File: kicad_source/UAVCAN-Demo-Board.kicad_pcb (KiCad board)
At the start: 2 copper layers, 91.4 x 50.8 mm, 38 parts, among them CN1 ARDUINO_NANO_33, CN2 691322310004, CN3 GH_SM04B-GHS-TB, CN4 GH_SM04B-GHS-TB, CN5 691322310004, CN6 691322310004, SW1 TAST_VER, U1 MCP2515, U2 SN65VHD232, U3 DS18B20, Y1 16 MHz

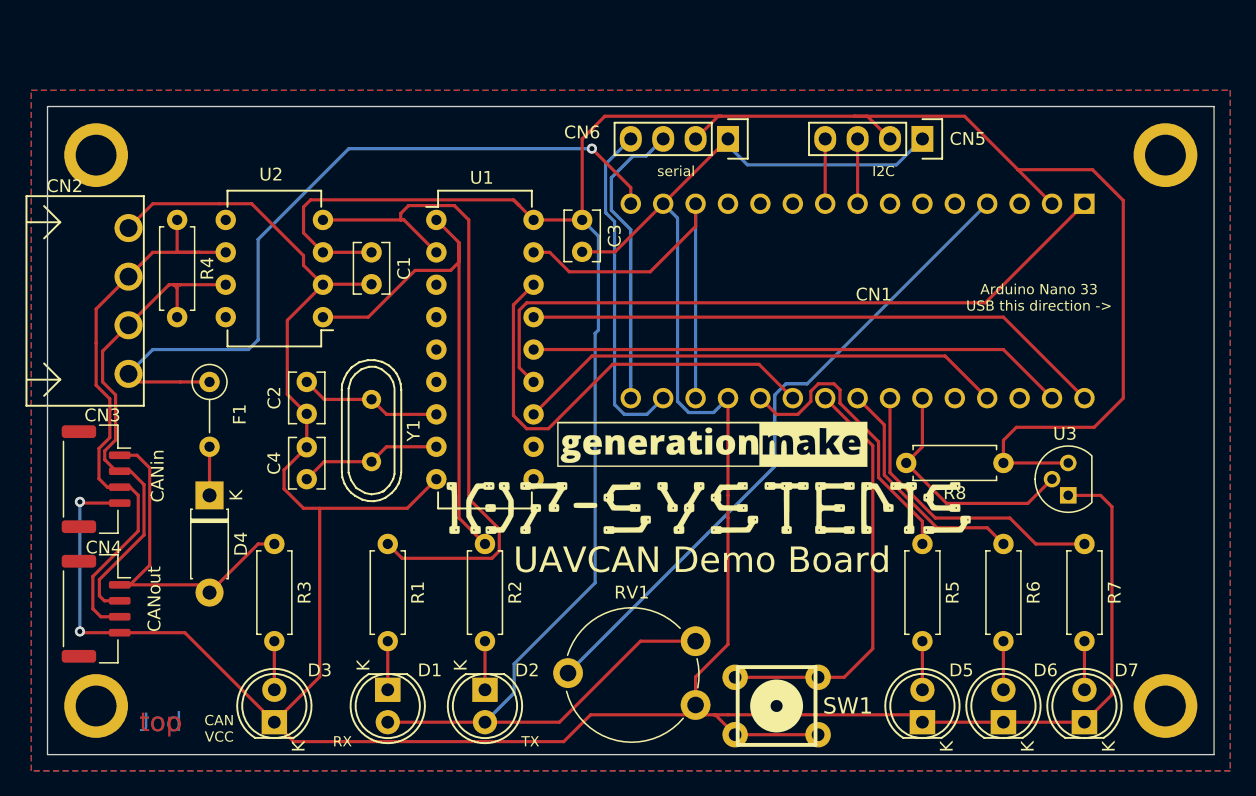
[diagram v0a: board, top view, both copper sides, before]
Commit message: updated schematic and layout, added dip switch for configuration, added measurement for CANVCC
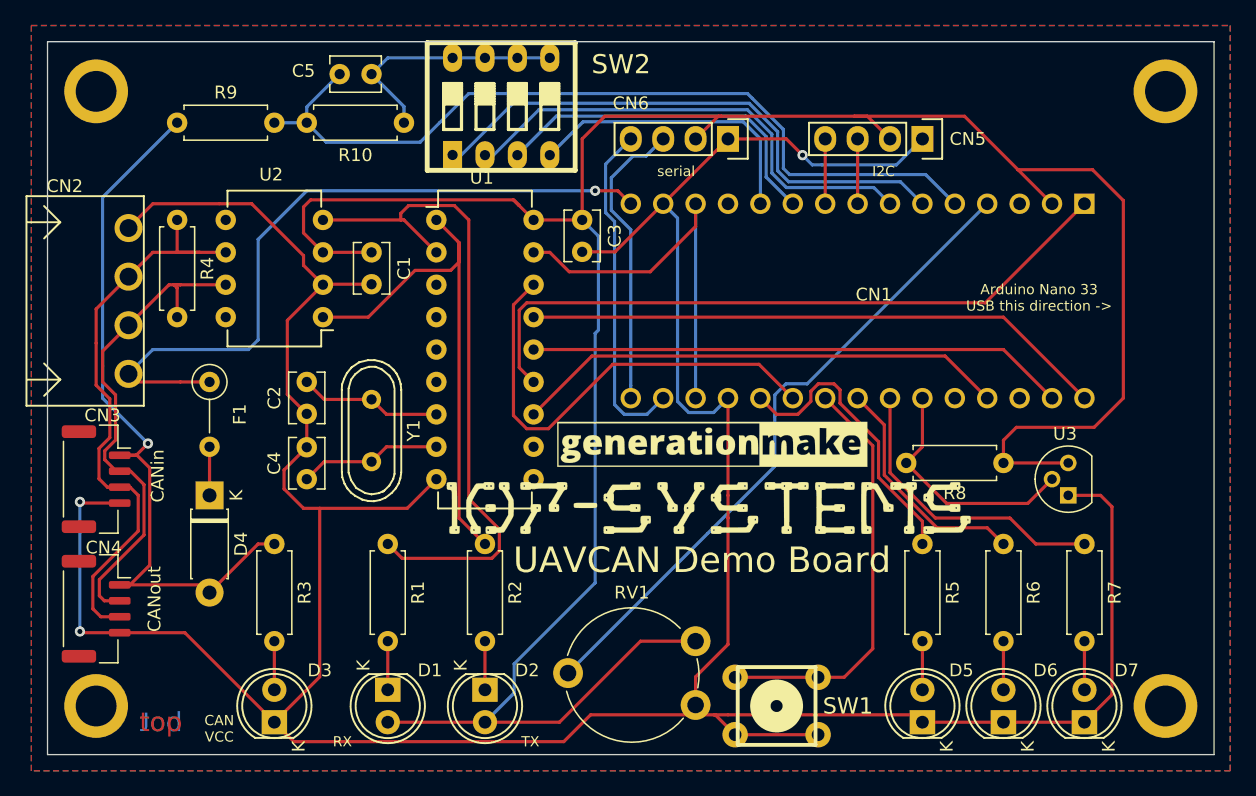
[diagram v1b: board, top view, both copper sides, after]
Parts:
- added C5: 100nF, Capacitor_THT:C_Disc_D3.8mm_W2.6mm_P2.50mm, F.Cu at (176.6, 31.8)
- added R10: 10k, Resistor_THT:R_Axial_DIN0207_L6.3mm_D2.5mm_P7.62mm_Horizontal, F.Cu at (174.0, 35.6)
- added R9: 10k, Resistor_THT:R_Axial_DIN0207_L6.3mm_D2.5mm_P7.62mm_Horizontal, F.Cu at (163.8, 35.6)
- added SW2: SW_DIP_x4, mechanical-switches:dip_4-300, F.Cu at (189.2, 34.3)
- moved MECH1 5.00 mm to (157.5, 33.1)
- moved MECH4 5.00 mm to (241.3, 33.1)
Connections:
- CN1 pad 10: (no net) -> /DIP_SW3
- CN1 pad 11: (no net) -> /DIP_SW4
- CN1 pad 5: (no net) -> /MEASURE_CANVCC
- CN1 pad 6: (no net) -> /DIP_SW1
- CN1 pad 7: (no net) -> /DIP_SW2
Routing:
- net /MEASURE_CANVCC: track 0.00 -> 65.8 mm
- net /DIP_SW1: track 0.00 -> 43.6 mm
- net /DIP_SW2: track 0.00 -> 38.1 mm
- net /CANVCC: track 27.3 -> 59.0 mm, vias 0 -> 1
- net /DIP_SW3: track 0.00 -> 27.6 mm
- net /DIP_SW4: track 0.00 -> 23.2 mm
- net GND: track 278.5 -> 297.5 mm, vias 2 -> 3
- net +5V: track 60.4 -> 57.0 mm
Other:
- board size 91.4 x 50.8 mm -> 91.4 x 55.9 mm

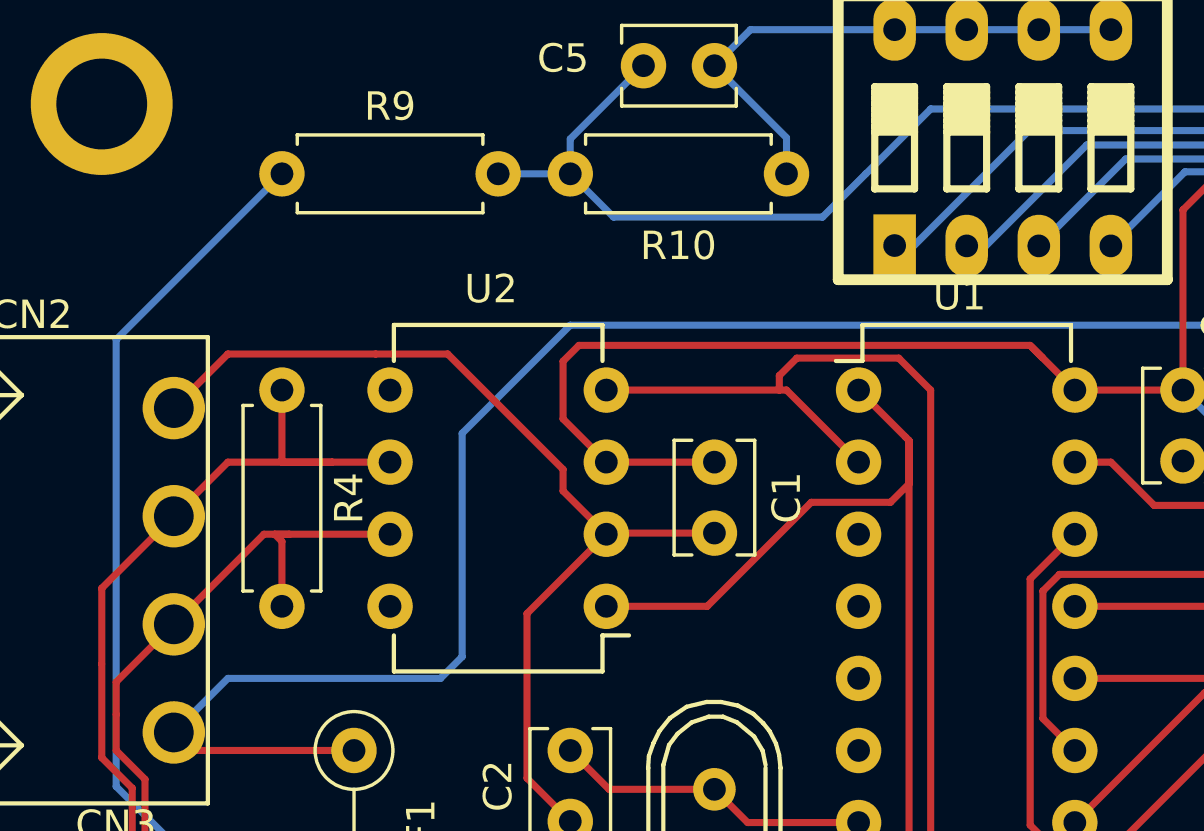
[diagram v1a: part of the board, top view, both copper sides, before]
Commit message: switched CAN transceiver to MCP2562 because of DIP package
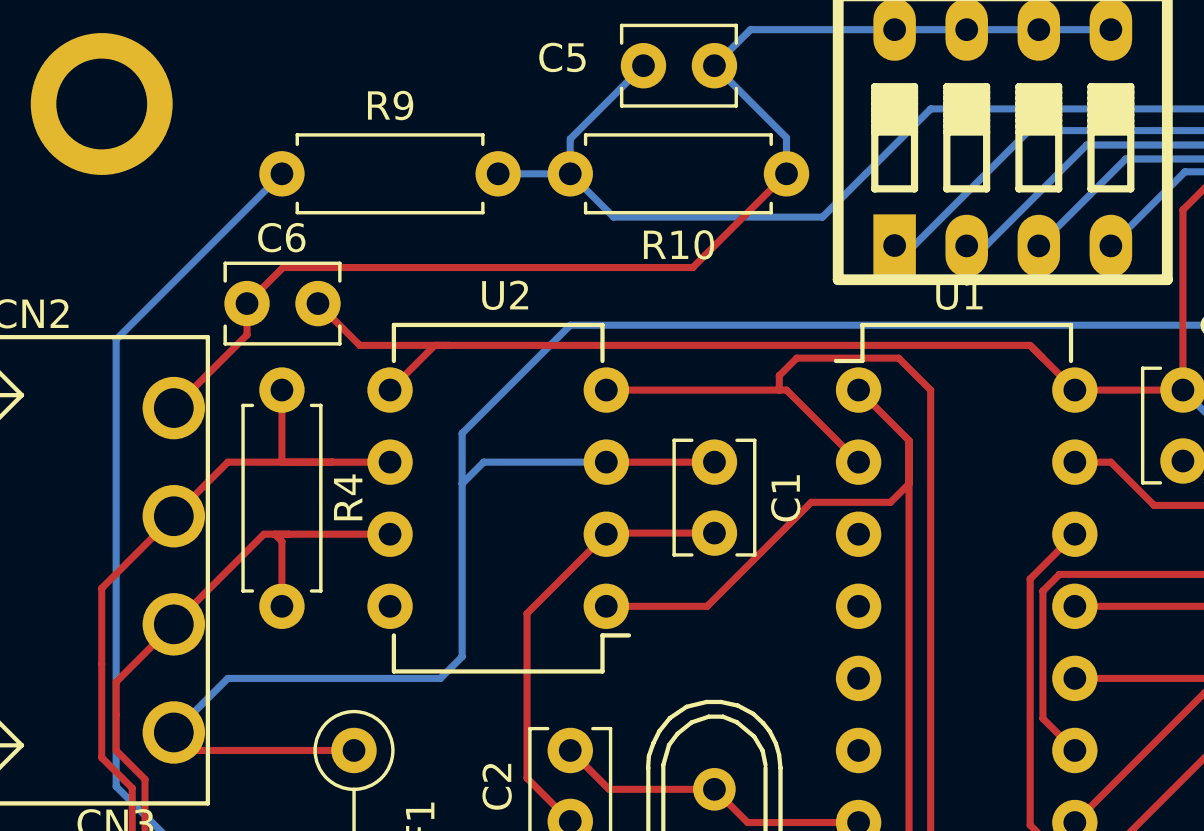
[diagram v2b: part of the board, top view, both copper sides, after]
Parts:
- added C6: 100nF, Capacitor_THT:C_Disc_D3.8mm_W2.6mm_P2.50mm, F.Cu at (165.1, 40.1)
- U2: value SN65VHD232 -> MCP2562-EP
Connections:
- C1 pad 1: +3V3 -> +5V
- U2 pad 3: +3V3 -> +5V
- U2 pad 5: (no net) -> +3V3
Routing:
- net +5V: track 57.0 -> 66.2 mm
- net GND: track 297.5 -> 304.1 mm
- net +3V3: track 197.0 -> 200.8 mm

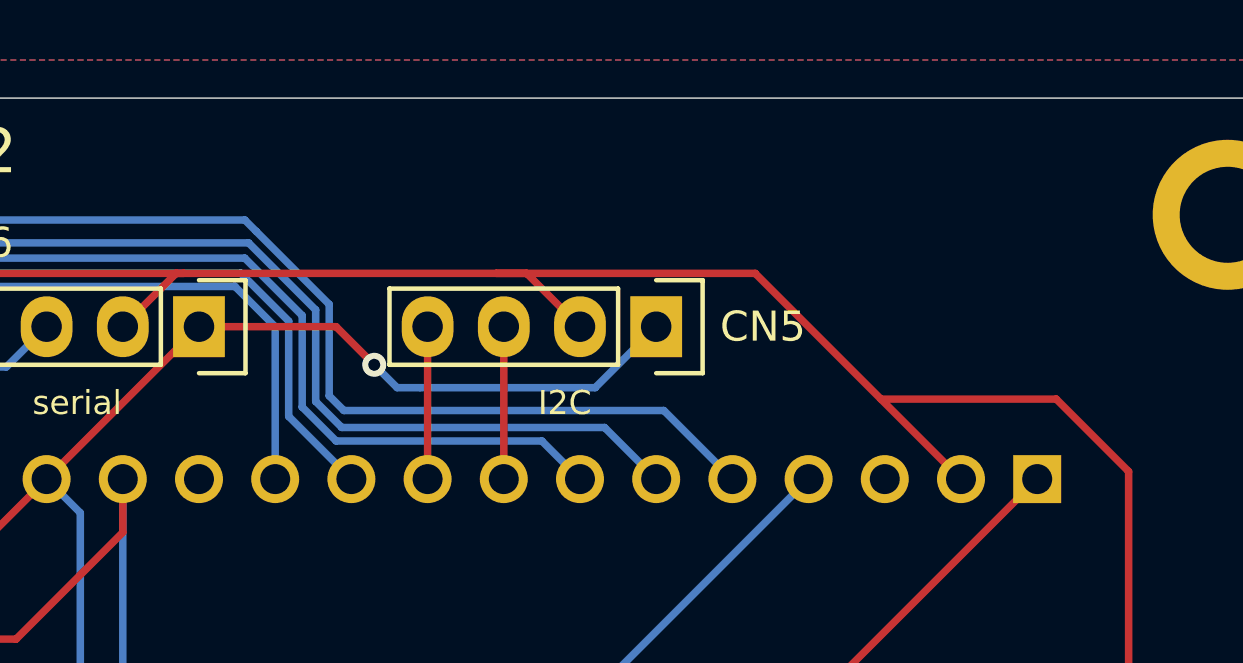
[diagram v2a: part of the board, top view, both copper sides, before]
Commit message: added Qwiic connector
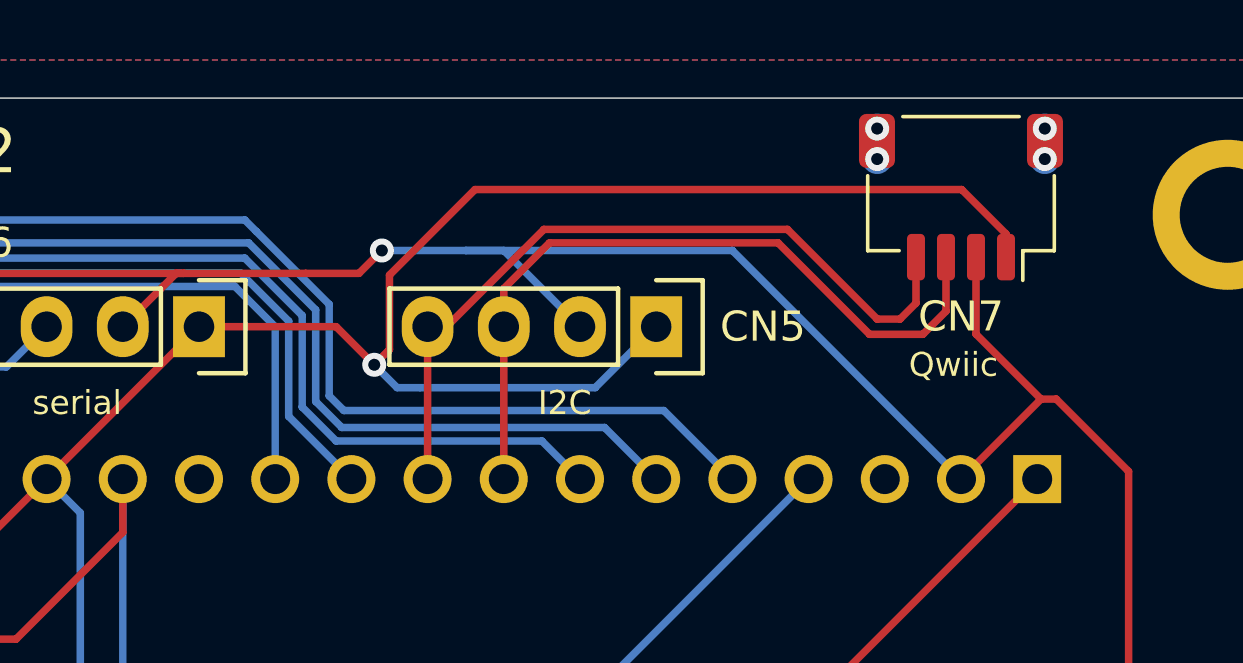
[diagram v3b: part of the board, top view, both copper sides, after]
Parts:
- added CN7: SM04B-SRSS-TB, Connector_JST:JST_SH_SM04B-SRSS-TB_1x04-1MP_P1.00mm_Horizontal, F.Cu at (232.4, 32.5)
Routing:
- net GND: track 304.1 -> 330.4 mm
- net /I2C_SCL: track 5.08 -> 25.7 mm
- net /I2C_SDA: track 5.08 -> 25.1 mm
- net +3V3: track 200.8 -> 206.8 mm, vias 0 -> 1
- net (no net): track 0.00 -> 2.03 mm, vias 0 -> 4
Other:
- board text added: "Qwiic"
